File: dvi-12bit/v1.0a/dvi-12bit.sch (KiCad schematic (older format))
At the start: 33 parts, among them J1 PMOD, J2 PMOD, J3 jmp, J4 5V, J5 jmp, J6 HDMI_A_1.4, U1 VREG_3V3, U2 TFP410

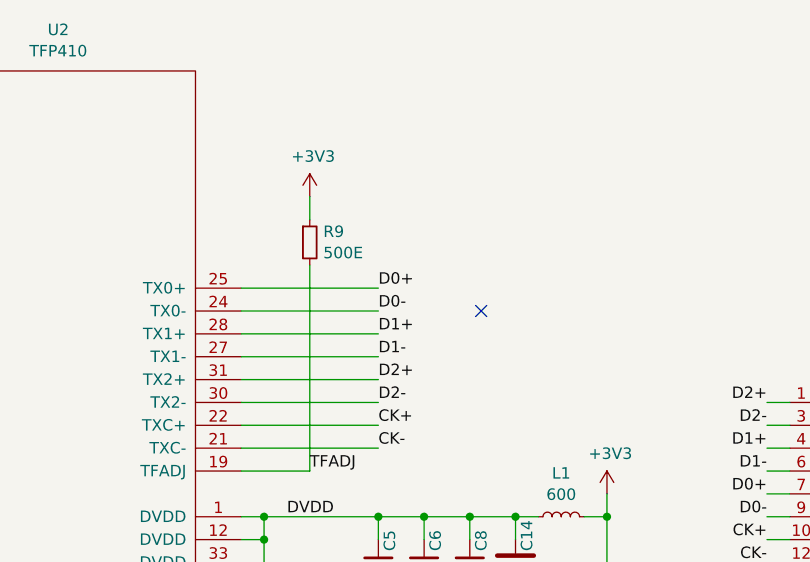
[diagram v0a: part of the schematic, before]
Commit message: A few minor fixes to the dvi PMODs.
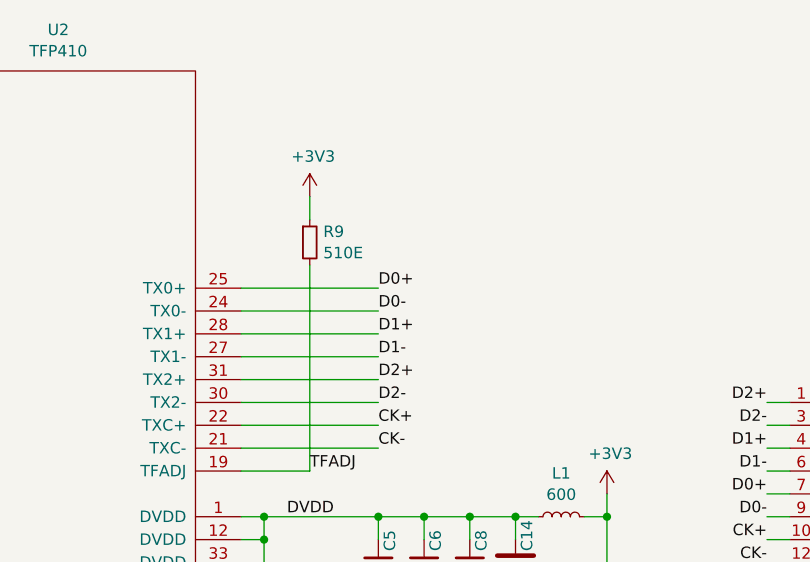
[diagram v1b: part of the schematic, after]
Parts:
- J4: Key conn-th-01in-6-2-hdr-ra -> conn-th-01in-2-1-rec
- J6: Key (none) -> conn-hdmi-10029449-111rlf
- L1, L2, L3: Key ind-0402-600 -> ferrite-0402-600
- R9: value 500E -> 510E; Key res-0402-500 -> res-0402-510
- U2: Key (none) -> ic-tqfp64-tfp410
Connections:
- no-connect marks 10 -> 9
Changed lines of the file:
@@
 F 3 "https://en.wikipedia.org/wiki/HDMI" H 9425 3700 50  0001 C CNN
 F 4 "ANY" H 9400 3700 50  0001 C CNN "Source"
+F 5 "conn-hdmi-10029449-111rlf" H 0   0   50  0001 C CNN "Key"
 	1    9400 3700
 	1    0    0    -1
@@
 F 3 "http://www.ti.com/lit/ds/symlink/tfp410.pdf" H 5850 1250 50  0001 C CNN
 F 4 "ANY" H 5800 3600 50  0001 C CNN "Source"
+F 5 "ic-tqfp64-tfp410" H 0   0   50  0001 C CNN "Key"
 	1    5800 3600
 	1    0    0    -1
@@
 P 6900 2200
 F 0 "R9" H 6959 2247 50  0000 L CNN
-F 1 "500E" H 6959 2154 50  0000 L CNN
+F 1 "510E" H 6959 2154 50  0000 L CNN
 F 2 "pkl_dipol:R_0402" H 6959 2107 60  0001 L CNN
 F 3 "" H 6900 2200 60  0000 C CNN
-F 4 "res-0402-500" H 6900 2200 50  0001 C CNN "Key"
+F 4 "res-0402-510" H 6900 2200 50  0001 C CNN "Key"
 F 5 "ANY" H 6900 2200 50  0001 C CNN "Source"
 	1    6900 2200
@@
 F 2 "pkl_dipol:L_0402" H 8049 3307 60  0001 L CNN
 F 3 "" V 8000 3400 60  0000 C CNN
-F 4 "ind-0402-600" H 8000 3400 50  0001 C CNN "Key"
+F 4 "ferrite-0402-600" H 8000 3400 50  0001 C CNN "Key"
 F 5 "ANY" H 8000 3400 50  0001 C CNN "Source"
 	1    8000 3400
@@
 F 2 "pkl_dipol:L_0402" H 8049 4207 60  0001 L CNN
 F 3 "" V 8000 4300 60  0000 C CNN
-F 4 "ind-0402-600" H 8000 4300 50  0001 C CNN "Key"
+F 4 "ferrite-0402-600" H 8000 4300 50  0001 C CNN "Key"
 F 5 "ANY" H 8000 4300 50  0001 C CNN "Source"
 	1    8000 4300
@@
 F 2 "pkl_dipol:L_0402" H 8049 5107 60  0001 L CNN
 F 3 "" V 8000 5200 60  0000 C CNN
-F 4 "ind-0402-600" H 8000 5200 50  0001 C CNN "Key"
+F 4 "ferrite-0402-600" H 8000 5200 50  0001 C CNN "Key"
 F 5 "ANY" H 8000 5200 50  0001 C CNN "Source"
 	1    8000 5200
@@
 F 2 "Connector_PinHeader_2.54mm:PinHeader_2x01_P2.54mm_Vertical" H 1800 2600 50  0001 C CNN
 F 3 "~" H 1800 2600 50  0001 C CNN
-F 4 "conn-th-01in-6-2-hdr-ra" H 1800 2600 50  0001 C CNN "Key"
+F 4 "conn-th-01in-2-1-rec" H 1800 2600 50  0001 C CNN "Key"
 F 5 "ANY" H 1800 2600 50  0001 C CNN "Source"
 	1    1800 2600
@@
 Wire Wire Line
 	6700 4700 6700 5000
-NoConn ~ 7650 2500
 Wire Wire Line
 	1500 4600 1500 3800
